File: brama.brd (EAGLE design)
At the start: 92.7 x 127.5 mm, 57 parts, among them IC1 AT90USB162A, J1 AVR_SPI_PRG_6OFFSET_PADS

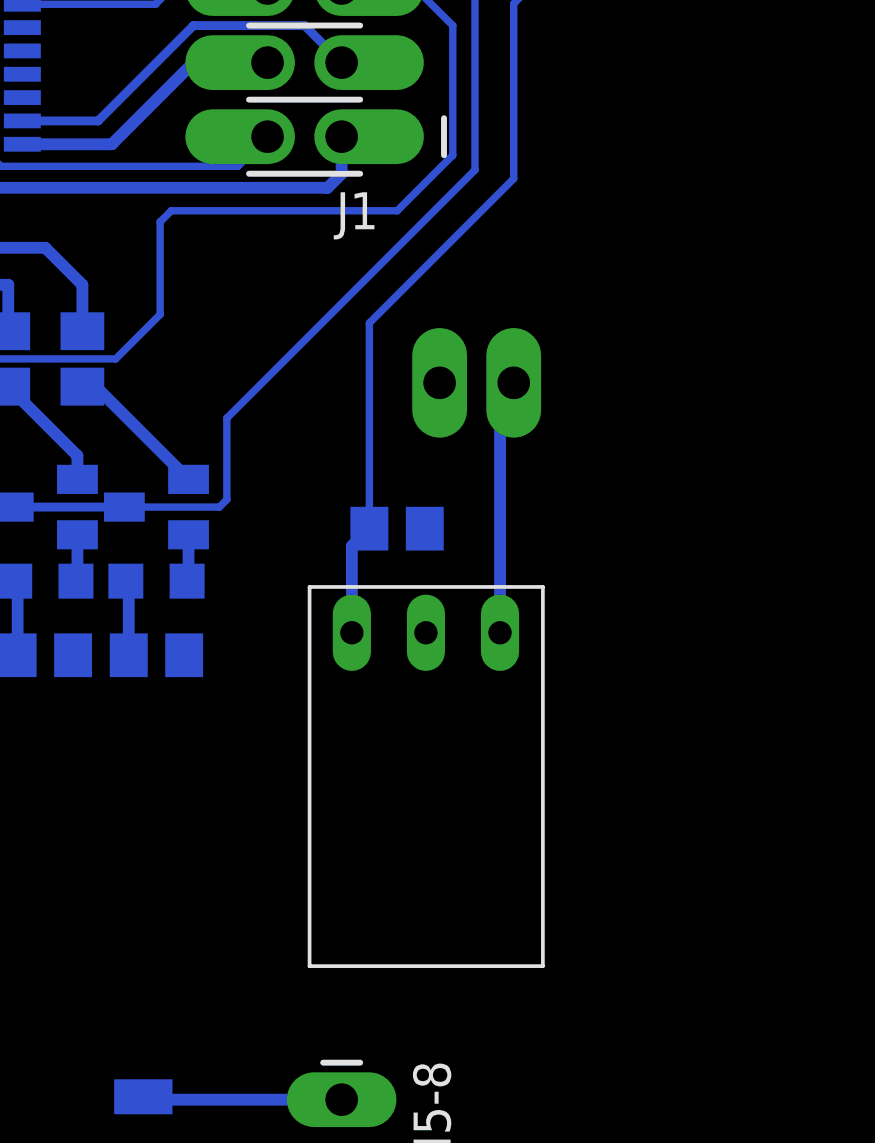
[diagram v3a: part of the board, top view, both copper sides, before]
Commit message: LM2704 Step-Up DC/DC Converter
http://www.ti.com.cn/general/cn/docs/lit/getliterature.tsp?genericPartNumber=lm2704&fileType=pdf
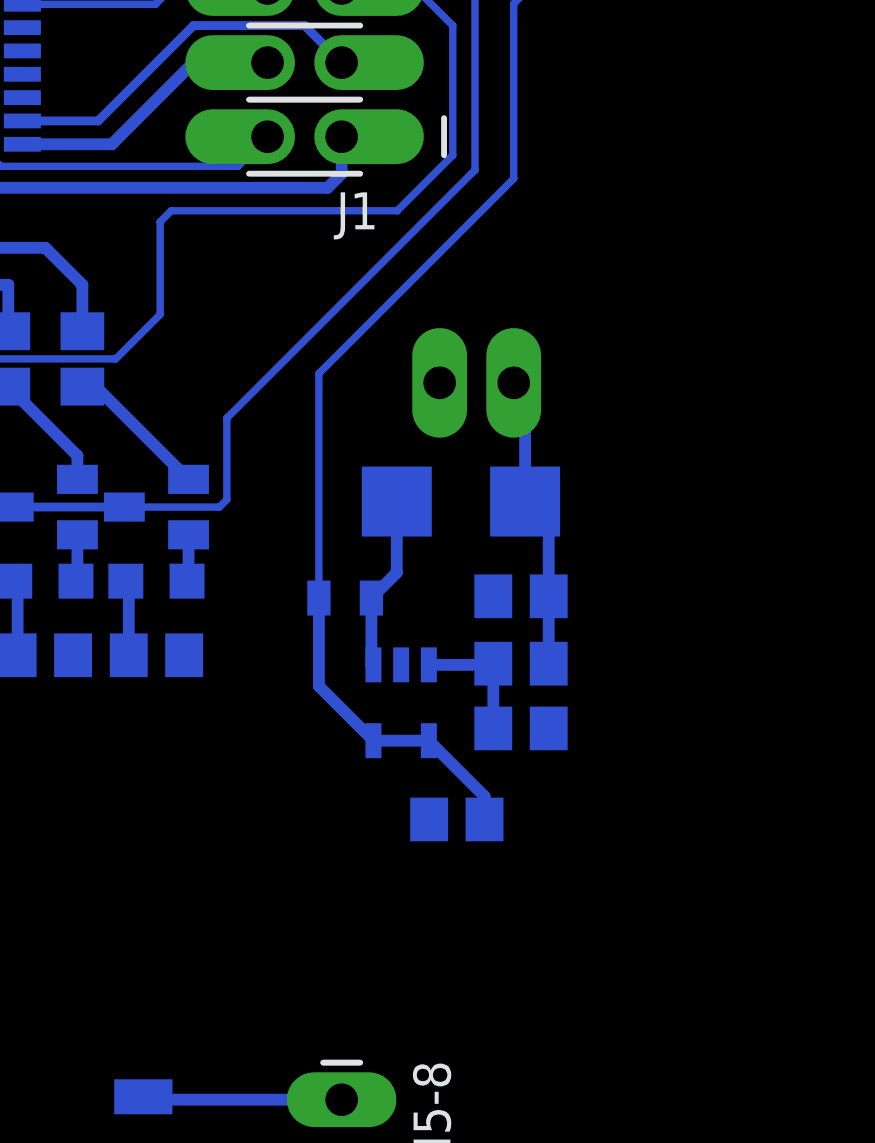
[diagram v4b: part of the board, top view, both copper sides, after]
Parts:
- added C8: 4,7uF, rcl:C0805
- added D1: (no value), SparkFun-DiscreteSemi:SMB-DIODE
- added L1: (no value), SparkFun-Passives:0805
- added R18: 240k, rcl:R0805
- added R19: 27k, rcl:R0805
- C7: value 33n -> 4,7uF
- U$6: value U3V12F12 -> LM2704MF-ADJ; device pololu DC-DC converters:THT -> Step-Up:SOT23-5
- moved U$6 10.3 mm to (40.1, 72.0), flipped to the bottom, turned to 180 degrees
- moved C7 10.2 mm to (42.0, 68.0)
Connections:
- new net N$31: D1.A, L1.2, U$6.SW
- new net N$34: R18.1, R19.2, U$6.FB
- net 12V: now also C8.1, D1.C, R18.2; no longer U$6.VOUT
- net 5V: now also C7.1, L1.1, U$6.!SHDN; no longer C7.2
- net GND: now also C7.2, C8.2, R19.1; no longer C7.1
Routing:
- net 5V: track 188.7 -> 199.0 mm
- net N$31: track 0.00 -> 6.03 mm
- net N$34: track 0.00 -> 4.47 mm
- net 12V: track 8.76 -> 10.8 mm
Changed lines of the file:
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@@
 <element name="U$4" library="holes" package="3,0" value="" x="86" y="110"/>
 <element name="U$5" library="holes" package="3,0" value="" x="6" y="-2"/>
-<element name="U$6" library="pololu DC-DC converters" package="THT" value="U3V12F12" x="45" y="63" rot="R90"/>
-<element name="C7" library="rcl" package="C0805" value="33n" x="40" y="78" rot="MR0"/>
 <element name="JP8" library="SparkFun-Connectors" package="1X02_LONGPADS" value="" x="44" y="83" rot="R180"/>
+<element name="U$6" library="Step-Up" package="SOT23-5" value="LM2704MF-ADJ" x="40.14" y="72.03000625" rot="MR180"/>
+<element name="L1" library="SparkFun-Passives" package="0805" value="" x="38.219965625" y="75.619865625" rot="MR180"/>
+<element name="C7" library="rcl" package="C0805" value="4,7uF" x="42.049878125" y="68.029834375" rot="MR0"/>
+<element name="C8" library="rcl" package="C0805" value="4,7uF" x="44.249871875" y="75.679809375" rot="MR0"/>
+<element name="R18" library="rcl" package="R0805" value="240k" x="44.24995" y="73.36990625" rot="MR180"/>
+<element name="R19" library="rcl" package="R0805" value="27k" x="44.249875" y="71.14979375" rot="MR0"/>
+<element name="D1" library="SparkFun-DiscreteSemi" package="SMB-DIODE" value="" x="42.18988125" y="78.9297625" rot="MR0"/>
 </elements>
 <signals>
@@
 <contactref element="JP4" pad="1"/>
 <contactref element="JP5" pad="1"/>
+<contactref element="JP8" pad="2"/>
+<contactref element="C7" pad="2"/>
+<contactref element="C8" pad="2"/>
 <contactref element="U$6" pad="GND"/>
-<contactref element="C7" pad="1"/>
-<contactref element="JP8" pad="2"/>
+<contactref element="R19" pad="1"/>
 </signal>
 <signal name="5V">
@@
 <wire x1="12.639" y1="97.475" x2="11.43" y2="97.475" width="0.254" layer="16"/>
 <wire x1="38.3286" y1="106.1212" x2="37.6174" y2="105.41" width="0.254" layer="16"/>
-<contactref element="U$6" pad="VIN"/>
-<contactref element="C7" pad="2"/>
-<wire x1="38.45" y1="74.43" x2="38.45" y2="77.4" width="0.4064" layer="16"/>
-<wire x1="38.45" y1="77.4" x2="39.05" y2="78" width="0.4064" layer="16"/>
-<wire x1="39.05" y1="78" x2="39.05" y2="85.05" width="0.254" layer="16"/>
-<wire x1="39.05" y1="85.05" x2="44" y2="90" width="0.254" layer="16"/>
+<wire x1="37.319965625" y1="83.319965625" x2="44" y2="90" width="0.254" layer="16"/>
 <wire x1="44" y1="90" x2="44" y2="96" width="0.254" layer="16"/>
 <wire x1="44" y1="96" x2="45" y2="97" width="0.254" layer="16"/>
@@
 <wire x1="71" y1="115" x2="31.716" y2="115" width="0.254" layer="16"/>
 <wire x1="31.716" y1="115" x2="30" y2="113.284" width="0.254" layer="16"/>
+<contactref element="L1" pad="1"/>
+<contactref element="U$6" pad="!SHDN"/>
+<contactref element="C7" pad="1"/>
+<contactref element="U$6" pad="VIN"/>
+<wire x1="39.19" y1="70.72990625" x2="37.319965625" y2="72.599940625" width="0.4064" layer="16"/>
+<wire x1="37.319965625" y1="72.599940625" x2="37.319965625" y2="75.619865625" width="0.4064" layer="16"/>
+<wire x1="41.09" y1="70.72990625" x2="42.999878125" y2="68.820028125" width="0.4064" layer="16"/>
+<wire x1="42.999878125" y1="68.820028125" x2="42.999878125" y2="68.029834375" width="0.4064" layer="16"/>
+<wire x1="39.19" y1="70.72990625" x2="41.09" y2="70.72990625" width="0.4064" layer="16"/>
+<wire x1="37.319965625" y1="83.319965625" x2="37.319965625" y2="75.619865625" width="0.254" layer="16"/>
 </signal>
 <signal name="RESET">
@@
 </signal>
 <signal name="12V">
-<contactref element="U$6" pad="VOUT"/>
 <contactref element="JP8" pad="1"/>
-<wire x1="43.53" y1="74.43" x2="43.53" y2="82.53" width="0.4064" layer="16"/>
 <wire x1="43.53" y1="82.53" x2="44" y2="83" width="0.4064" layer="16"/>
+<contactref element="D1" pad="C"/>
+<contactref element="R18" pad="2"/>
+<contactref element="C8" pad="1"/>
+<wire x1="45.19995" y1="73.36990625" x2="45.199871875" y2="73.369984375" width="0.4064" layer="16"/>
+<wire x1="45.199871875" y1="73.369984375" x2="45.199871875" y2="75.679809375" width="0.4064" layer="16"/>
+<wire x1="45.199871875" y1="75.679809375" x2="45.199871875" y2="78.119771875" width="0.4064" layer="16"/>
+<wire x1="45.199871875" y1="78.119771875" x2="44.38988125" y2="78.9297625" width="0.4064" layer="16"/>
+<wire x1="44.38988125" y1="78.9297625" x2="44.38988125" y2="82.61011875" width="0.4064" layer="16"/>
+<wire x1="44.38988125" y1="82.61011875" x2="44" y2="83" width="0.4064" layer="16"/>
+</signal>
+<signal name="N$34">
+<contactref element="R19" pad="2"/>
+<contactref element="R18" pad="1"/>
+<contactref element="U$6" pad="FB"/>
+<wire x1="43.29995" y1="73.36990625" x2="43.299875" y2="73.36990625" width="0.4064" layer="16"/>
+<wire x1="43.299875" y1="73.36990625" x2="43.299875" y2="71.14979375" width="0.4064" layer="16"/>
+<wire x1="41.09" y1="73.33010625" x2="43.29995" y2="73.33010625" width="0.4064" layer="16"/>
+<wire x1="43.29995" y1="73.33010625" x2="43.29995" y2="73.36990625" width="0.4064" layer="16"/>
+</signal>
+<signal name="N$31">
+<contactref element="L1" pad="2"/>
+<contactref element="D1" pad="A"/>
+<contactref element="U$6" pad="SW"/>
+<wire x1="39.19" y1="73.33010625" x2="39.119965625" y2="73.33010625" width="0.4064" layer="16"/>
+<wire x1="39.119965625" y1="73.33010625" x2="39.119965625" y2="75.619865625" width="0.4064" layer="16"/>
+<wire x1="39.119965625" y1="75.619865625" x2="39.98988125" y2="76.48978125" width="0.4064" layer="16"/>
+<wire x1="39.98988125" y1="76.48978125" x2="39.98988125" y2="78.9297625" width="0.4064" layer="16"/>
 </signal>
 </signals>

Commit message: pdf
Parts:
- moved C5 10.2 mm to (30.9, 114.0)
- moved C7 10.2 mm to (42.0, 78.2)
- moved D1 10.2 mm to (42.2, 89.1)
- moved JP2 10.2 mm to (30.6, 111.0)
- moved JP5 10.2 mm to (34.5, 113.3)
- moved Q1 10.2 mm to (31.8, 88.9)
- moved Q2 10.2 mm to (27.9, 88.9)
- moved Q3 10.2 mm to (24.1, 88.9)
- moved Q4 10.2 mm to (20.3, 88.9)
- moved Q5 10.2 mm to (16.5, 88.9)
- moved Q6 10.2 mm to (12.7, 88.9)
- moved R13 10.2 mm to (19.3, 83.1)
- moved R14 10.2 mm to (15.5, 83.1)
- moved R2 10.2 mm to (10.8, 102.9)
- moved R3 10.2 mm to (13.3, 97.8)
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
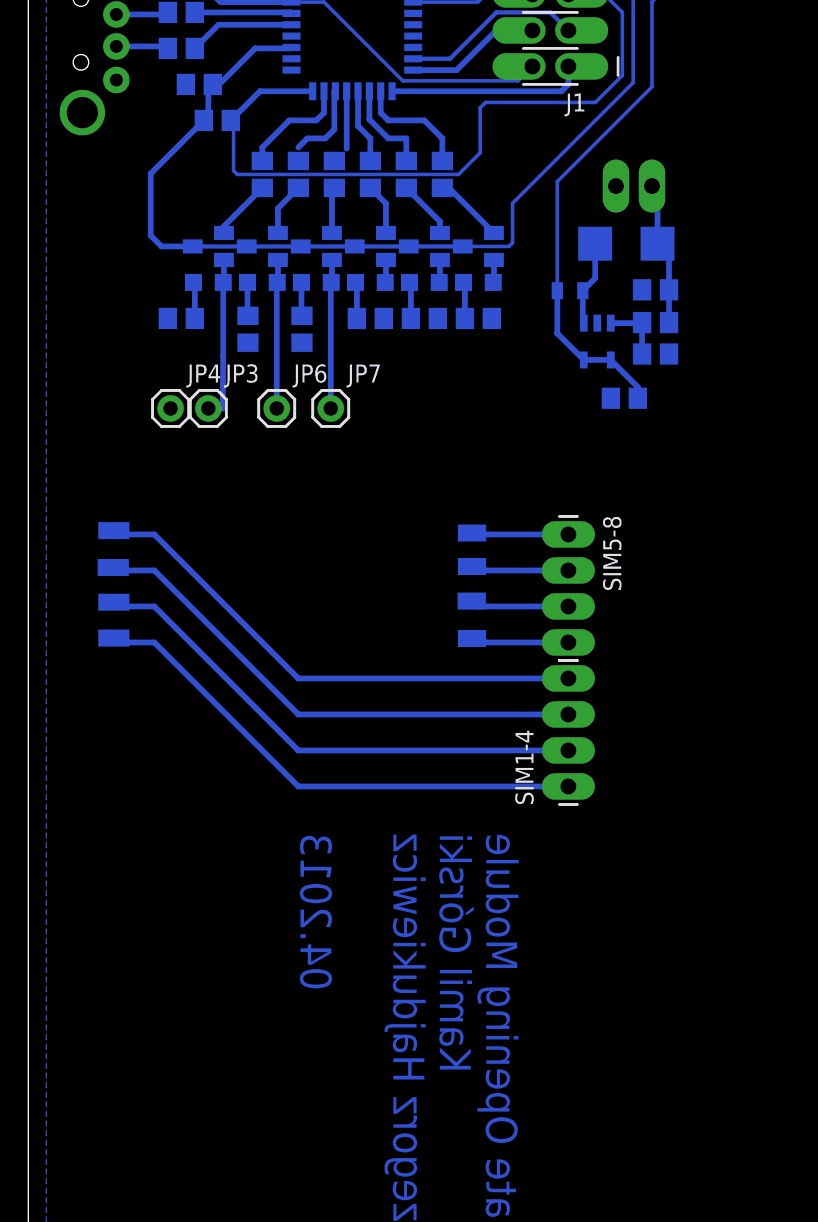
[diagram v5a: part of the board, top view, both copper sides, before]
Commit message: L7805 Added
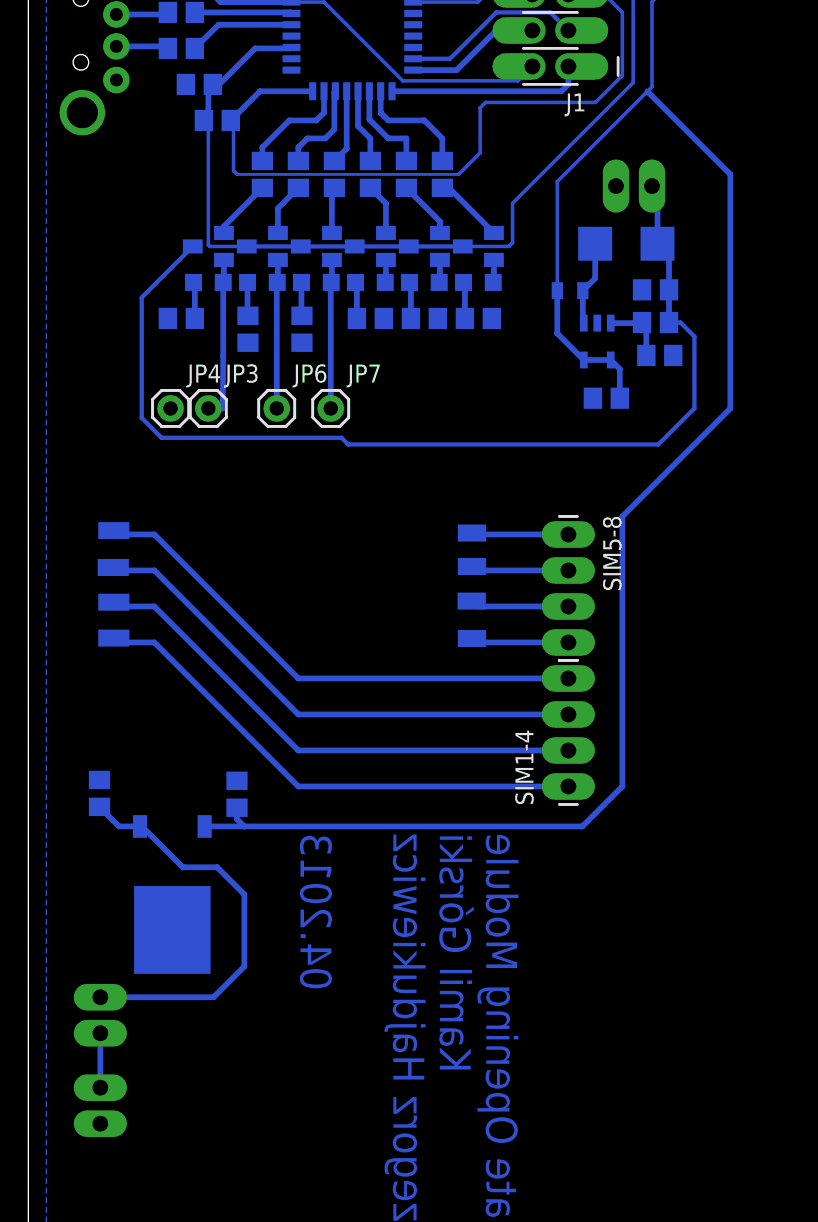
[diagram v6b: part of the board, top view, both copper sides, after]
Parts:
- added C10: 100n, rcl:C0805
- added C9: 330n, rcl:C0805
- added IC3: 7806DT, linear:TO252
- added JP10, JP9: (no value), SparkFun-Connectors:1X02_LONGPADS
- R15: value 100 -> 470
- moved C7 1.27 mm to (40.8, 78.2)
- moved R19 0.32 mm to (44.5, 81.2)
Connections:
- new net VIN: C9.1, IC3.1, JP10.1
- new net VIN_S: JP10.2, JP9.2
- net 12V: now also Q6.3
- net 3V3: no longer Q6.3
- net 5V: now also C10.1, IC3.2
- net GND: now also C10.2, C9.2, IC3.3, JP9.1
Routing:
- net 5V: track 199.0 -> 285.3 mm
- net 12V: track 10.8 -> 72.5 mm
- net VIN: track 0.00 -> 29.0 mm
- net 3V3: track 155.6 -> 150.5 mm
- net VIN_S: track 0.00 -> 3.84 mm
- net BUTTON1: track 4.05 -> 5.28 mm
- net BUTTON2: track 5.79 -> 6.74 mm

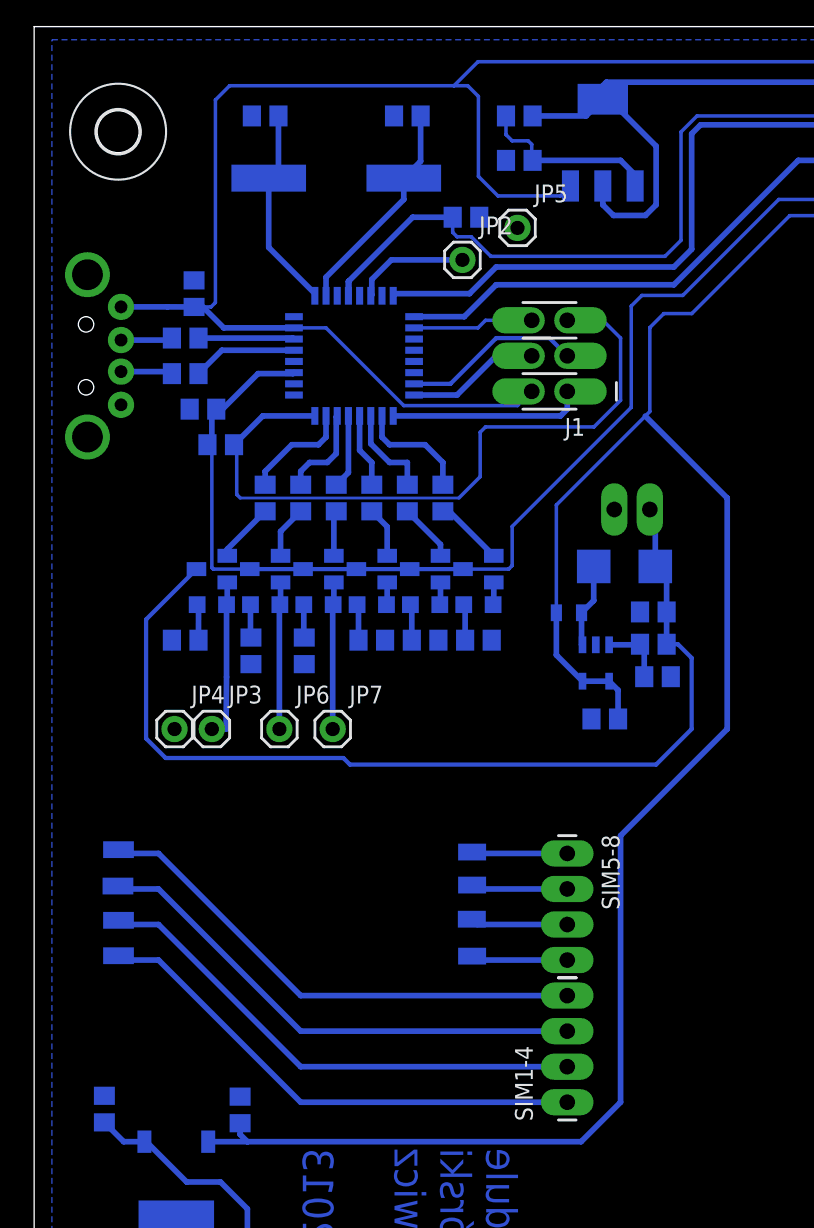
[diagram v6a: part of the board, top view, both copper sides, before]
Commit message: USB socket Change
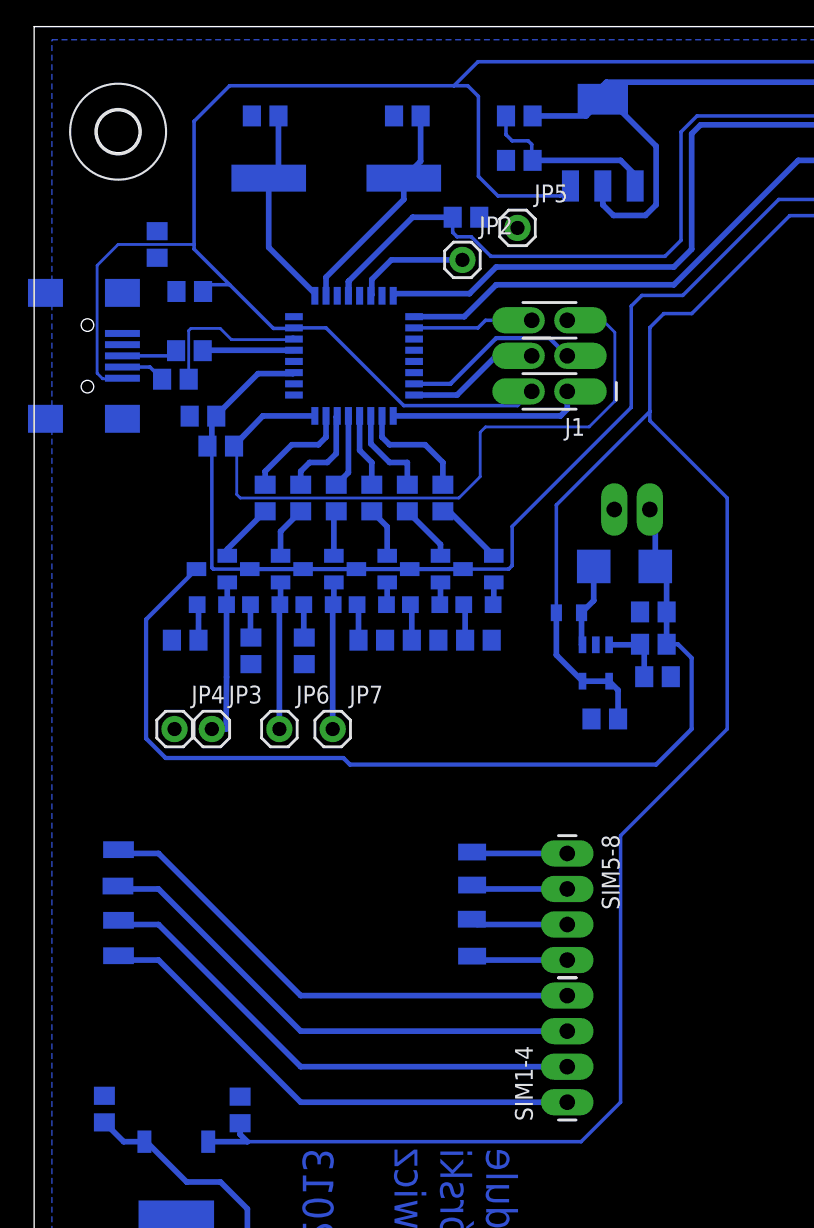
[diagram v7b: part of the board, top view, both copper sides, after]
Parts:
- added R20: 0, rcl:R0805
- C4: value 10u -> 22p
- JP1: value USB-A-H -> USBSMD; device SparkFun-Connectors:USB-A-H -> SparkFun-Connectors:USB-MINIB
- moved R1 3.02 mm to (10.1, 102.5)
- moved R2 1.67 mm to (11.1, 104.5)
- moved C1 0.50 mm to (12.1, 99.8)
- moved C4 0.35 mm to (11.1, 108.7), turned to 180 degrees
- moved R3 0.10 mm to (13.3, 97.7)
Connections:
- net 5V: now also C4.2; no longer C4.1
- net GND: now also C4.1, R20.1, R20.2; no longer C4.2
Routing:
- net 5V: track 285.3 -> 296.5 mm
- net N$1: track 6.85 -> 11.5 mm
- net N$2: track 7.51 -> 6.52 mm

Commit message: nowy druk
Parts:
- moved C10 4.02 mm to (10.9, 51.5)
- moved JP8 0.97 mm to (44.9, 93.5), turned to 0 degrees
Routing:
- net 5V: track 296.5 -> 314.5 mm
- net VIN: track 29.0 -> 17.0 mm
